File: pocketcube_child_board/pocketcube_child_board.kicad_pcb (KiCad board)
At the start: 2 copper layers, 50 x 50 mm, 7 parts, among them J1 M55-7102042R, U1 SI3477DV-T1-GE3

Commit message: Pushing Board sizes
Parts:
- removed the C1 at (99.2, 80.1)
- removed the J1 at (131.2, 82.3)
- removed the MOD1 at (110.7, 82.0)
- removed the U1 at (124.0, 68.5)
- added C1: 100nF, Capacitor_SMD:C_0402_1005Metric_Pad0.74x0.62mm_HandSolder, F.Cu at (125.3, 73.2)
- added C1: 100nF, Capacitor_SMD:C_0402_1005Metric_Pad0.74x0.62mm_HandSolder, F.Cu at (235.8, 63.3)
- added C2: 47uF, Capacitor_SMD:C_1206_3216Metric_Pad1.33x1.80mm_HandSolder, F.Cu at (225.1, 68.5)
- added C3: 47uF, Capacitor_SMD:C_1206_3216Metric_Pad1.33x1.80mm_HandSolder, F.Cu at (212.1, 59.7)
- added C4: 47uF, Capacitor_SMD:C_1206_3216Metric_Pad1.33x1.80mm_HandSolder, F.Cu at (220.3, 45.3)
- added C5: 47uF, Capacitor_SMD:C_1206_3216Metric_Pad1.33x1.80mm_HandSolder, F.Cu at (236.3, 52.0)
- added H1: MountingHole_Pad, MountingHole:MountingHole_2.2mm_M2_Pad_TopBottom, F.Cu at (204.3, 37.5)
- added H2: MountingHole_Pad, MountingHole:MountingHole_2.2mm_M2_Pad_TopBottom, F.Cu at (244.2, 37.5)
- added H3: MountingHole_Pad, MountingHole:MountingHole_2.2mm_M2_Pad_TopBottom, F.Cu at (204.3, 77.4)
- added H4: MountingHole_Pad, MountingHole:MountingHole_2.2mm_M2_Pad_TopBottom, F.Cu at (244.2, 77.4)
- added J1: M55-7102042R, inspirefly:HARWIN_M55-7102042R, F.Cu at (157.3, 75.4)
- added J1: M55-7102642R, inspirefly:HARWIN_M55-7102642R, F.Cu at (224.3, 74.8)
- added J2: M55-7101242R, inspirefly:HARWIN_M55-7101242R, F.Cu at (206.1, 55.5)
- added J3: M55-7101242R, inspirefly:HARWIN_M55-7101242R, F.Cu at (224.3, 39.3)
- added J4: M55-7101242R, inspirefly:HARWIN_M55-7101242R, F.Cu at (242.4, 55.5)
- added MOD1: RFM98W-433S2, inspirefly:XCVR_RFM98W-433S2, F.Cu at (224.1, 56.4)
- added MOD1: RFM98W-433S2, inspirefly:RFM98W-433S2, F.Cu at (136.8, 75.1)
- added R1: 100K, Resistor_SMD:R_0402_1005Metric_Pad0.72x0.64mm_HandSolder, F.Cu at (235.8, 61.3)
- added U1: SI3477DV-T1-GE3, inspirefly:SOT_V-T1-GE3_VIS, F.Cu at (150.1, 61.6)
- added U1: SI3477DV-T1-GE3, inspirefly:SOT_V-T1-GE3_VIS, F.Cu at (238.1, 67.6)
- AE1: moved to B.Cu
- moved AE1 107.4 mm to (202.1, 65.3), turned to -90 degrees
- moved R_BURN1 27.0 mm to (146.1, 61.8)
- moved R_PULLUP1 27.0 mm to (149.8, 64.1)
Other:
- board size 50 x 50 mm -> 133.6 x 52.6 mm
- board text added: "To +X"
- board text added: "To -X"
- board text added: "To -Y"
- board text added: "To Backplane"

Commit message: Antenna location changes
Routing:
- net GND: track 61.0 -> 55.9 mm, vias 40 -> 39
- added copper zone on In1.Cu, net GND
- added copper zone on In2.Cu, net GND
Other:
- copper layers 2 -> 4
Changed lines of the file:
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@@
 	(layers
 		(0 "F.Cu" signal)
+		(4 "In1.Cu" signal)
+		(6 "In2.Cu" signal)
 		(2 "B.Cu" signal)
 		(9 "F.Adhes" user "F.Adhesive")
@@
 	)
 	(setup
+		(stackup
+			(layer "F.SilkS"
+				(type "Top Silk Screen")
+			)
+			(layer "F.Paste"
+				(type "Top Solder Paste")
+			)
+			(layer "F.Mask"
+				(type "Top Solder Mask")
+				(thickness 0.01)
+			)
+			(layer "F.Cu"
+				(type "copper")
+				(thickness 0.035)
+			)
+			(layer "dielectric 1"
+				(type "prepreg")
+				(thickness 0.1)
+				(material "FR4")
+				(epsilon_r 4.5)
+				(loss_tangent 0.02)
+			)
+			(layer "In1.Cu"
+				(type "copper")
+				(thickness 0.035)
+			)
+			(layer "dielectric 2"
+				(type "core")
+				(thickness 1.24)
+				(material "FR4")
+				(epsilon_r 4.5)
+				(loss_tangent 0.02)
+			)
+			(layer "In2.Cu"
+				(type "copper")
+				(thickness 0.035)
+			)
+			(layer "dielectric 3"
+				(type "prepreg")
+				(thickness 0.1)
+				(material "FR4")
+				(epsilon_r 4.5)
+				(loss_tangent 0.02)
+			)
+			(layer "B.Cu"
+				(type "copper")
+				(thickness 0.035)
+			)
+			(layer "B.Mask"
+				(type "Bottom Solder Mask")
+				(thickness 0.01)
+			)
+			(layer "B.Paste"
+				(type "Bottom Solder Paste")
+			)
+			(layer "B.SilkS"
+				(type "Bottom Silk Screen")
+			)
+			(copper_finish "None")
+			(dielectric_constraints no)
+		)
 		(pad_to_mask_clearance 0)
 		(allow_soldermask_bridges_in_footprints no)
@@
 	)
 	(segment
-		(start 125.33 70.0825)
-		(end 124.53 70.0825)
-		(width 0.2)
-		(layer "F.Cu")
-		(net 3)
-	)
-	(segment
 		(start 122.63 65.0825)
 		(end 123.38 65.8325)
@@
 	)
 	(segment
-		(start 125.33 70.0825)
-		(end 125.33 72.5825)
-		(width 0.2)
-		(layer "F.Cu")
-		(net 3)
-	)
-	(segment
 		(start 151.5125 73.465)
 		(end 150.63 72.5825)
@@
 	)
 	(segment
-		(start 127.13 70.0825)
-		(end 125.33 70.0825)
-		(width 0.2)
-		(layer "F.Cu")
-		(net 3)
-	)
-	(segment
 		(start 146.88 65.8325)
 		(end 147.63 66.5825)
@@
 	)
 	(via
-		(at 124.53 70.0825)
-		(size 0.6)
-		(drill 0.3)
-		(layers "F.Cu" "B.Cu")
-		(free yes)
-		(net 3)
-	)
-	(via
 		(at 118.63 61.5825)
 		(size 0.6)
@@
 		(net 3)
 		(net_name "GND")
-		(layers "F.Cu" "B.Cu")
+		(layers "F.Cu" "B.Cu" "In1.Cu" "In2.Cu")
 		(hatch edge 0.5)
 		(priority 3)

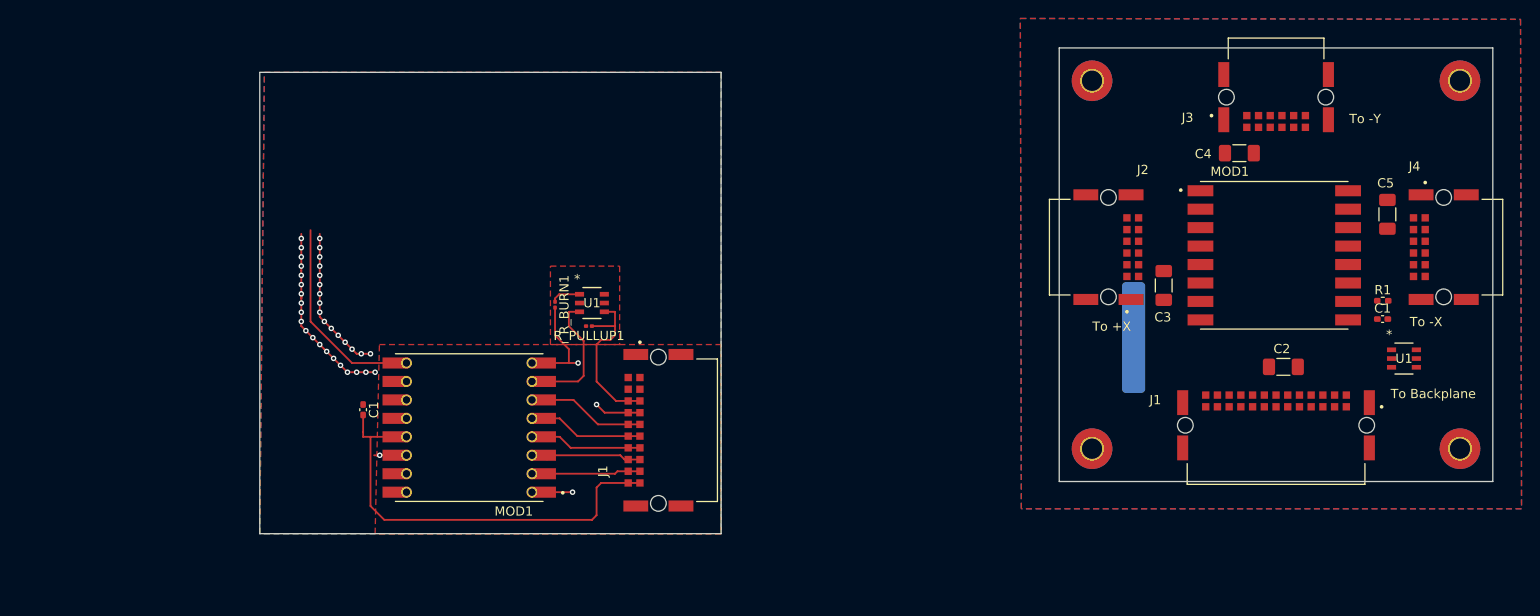
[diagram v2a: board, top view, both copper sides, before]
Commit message: updated antenna traces
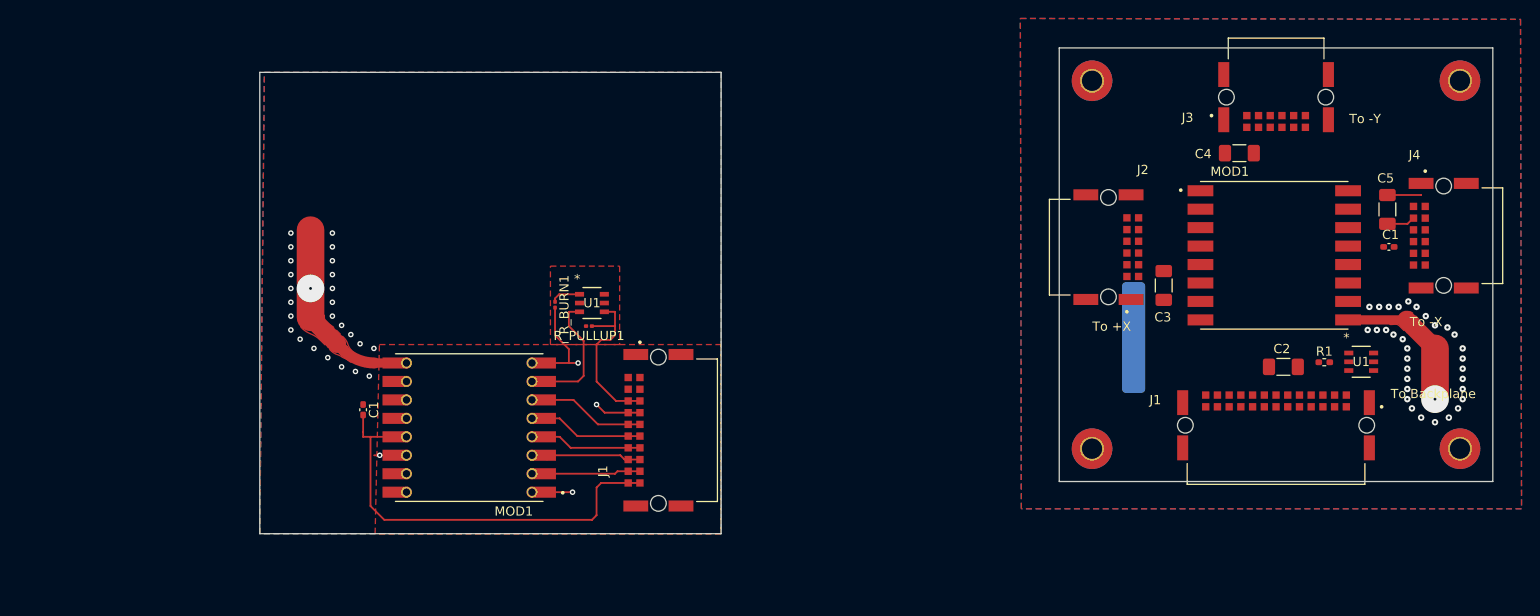
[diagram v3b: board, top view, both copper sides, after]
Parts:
- moved R1 9.20 mm to (229.5, 68.0)
- moved C1 7.85 mm to (236.5, 55.5)
- moved U1 4.65 mm to (233.5, 67.9)
- moved J4 1.24 mm to (242.4, 54.3)
- moved C5 0.53 mm to (236.3, 51.4)
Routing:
- net GND: track 55.9 -> 22.3 mm, vias 39 -> 60
- net /ANTENNA_TRACE: track 21.0 -> 37.8 mm, vias 0 -> 2
- net EXTERNAL_VOLTAGE: track 0.00 -> 3.10 mm
- added copper zone on F.Cu, net /ANTENNA_TRACE

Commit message: stuff from HITT
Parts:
- removed the C1 at (125.3, 73.2)
- removed the J1 at (157.3, 75.4)
- removed the MOD1 at (136.8, 75.1)
- removed R_BURN1: R, Resistor_SMD:R_0201_0603Metric
- removed R_PULLUP1: 10k, Resistor_SMD:R_0201_0603Metric
- removed the U1 at (150.1, 61.6)
- moved U1 3.65 mm to (237.2, 67.9)
- moved C1 2.00 mm to (236.5, 57.5)
- moved R1 1.80 mm to (230.5, 66.5)
- moved C5 1.50 mm to (236.3, 52.9)
- moved C2 1.13 mm to (223.9, 68.5)
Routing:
- net GND: track 22.3 -> 149.1 mm, vias 60 -> 13
- net 3.3V: track 46.6 -> 0.00 mm
- net /ANTENNA_TRACE: track 37.8 -> 0.00 mm, vias 2 -> 0
- net EXTERNAL_VOLTAGE: track 3.10 -> 24.0 mm
- net 4.2V: track 18.2 -> 0.00 mm
- net PMOS_GATE: track 13.4 -> 0.00 mm
- net MOSI: track 11.6 -> 0.00 mm
- net RFM_RESET: track 11.6 -> 0.00 mm
- net MISO: track 11.5 -> 0.00 mm
- net CS: track 11.3 -> 0.00 mm
- net CLK: track 11.0 -> 0.00 mm
- net BAT_VOLTAGE: track 0.00 -> 8.28 mm
- net Net-(R_BURN1-Pad1): track 3.20 -> 0.00 mm
- net +3.3V: track 0.00 -> 2.54 mm
- net unconnected-(MOD1-DIO0-Pad14): track 2.30 -> 0.00 mm, vias 1 -> 0
- removed copper zone on F.Cu, net /ANTENNA_TRACE
- removed copper zone on F.Cu, net 3.3V
- removed copper zone on F.Cu, net 4.2V
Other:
- board size 133.6 x 52.6 mm -> 47 x 47 mm

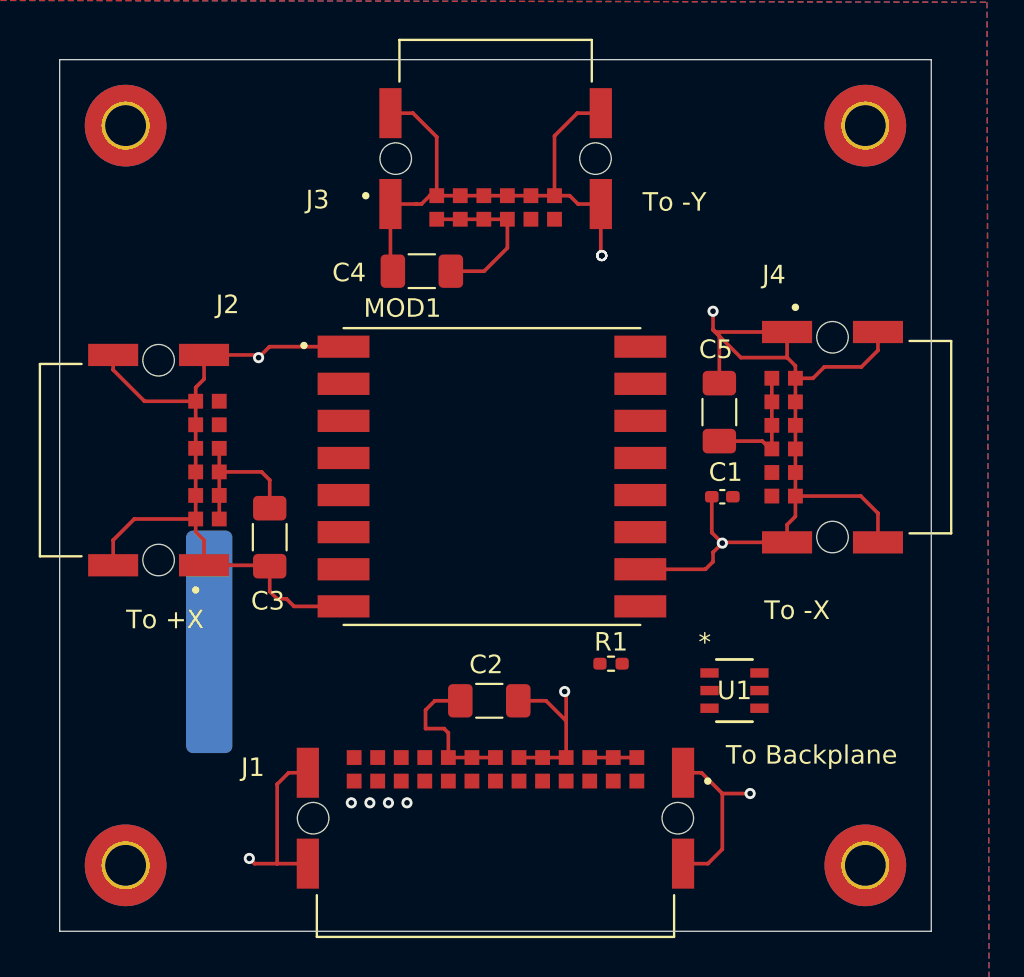
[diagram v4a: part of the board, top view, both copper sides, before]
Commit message: 4 layer board routing
2 ground layers between front and backplane to increase rf performance, may need to use for routing though
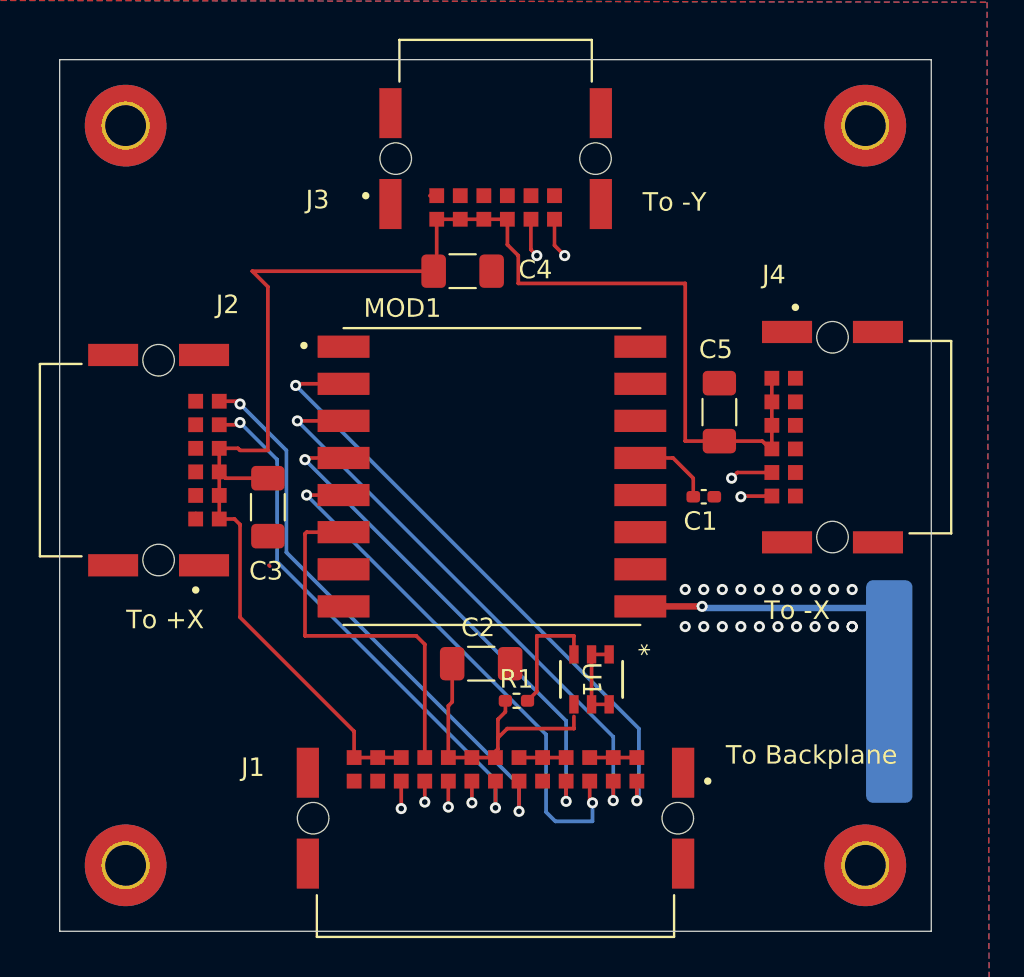
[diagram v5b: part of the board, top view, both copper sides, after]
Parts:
- moved AE1 50.2 mm to (252.2, 68.0), turned to 90 degrees
- moved U1 7.73 mm to (229.4, 67.3), turned to -90 degrees
- moved R1 5.48 mm to (225.4, 68.5)
- moved C4 2.20 mm to (222.5, 45.3), turned to 180 degrees
- moved C2 2.05 mm to (223.5, 66.5)
- moved C3 1.62 mm to (212.0, 58.1)
- moved C1 1.00 mm to (235.5, 57.5), turned to 180 degrees
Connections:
- J1 pad A1: ANT_SPI2_MOSI -> ANT_SPI2_MISO
- J1 pad A2: ANT_SPI2_MISO -> ANT_SPI2_MOSI
- J1 pad B10: EXTERNAL_VOLTAGE -> RFM_RESET
- J1 pad B13: RFM_RESET -> EXTERNAL_VOLTAGE
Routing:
- net GND: track 149.1 -> 3.94 mm, vias 13 -> 21
- net EXTERNAL_VOLTAGE: track 24.0 -> 84.5 mm
- net ANT_SPI2_MISO: track 0.00 -> 33.9 mm, vias 0 -> 2
- net ANT_SPI2_MOSI: track 0.00 -> 31.1 mm, vias 0 -> 2
- net I2C1_SDA: track 0.00 -> 31.0 mm, vias 0 -> 2
- net ANT_SPI2_NSS: track 0.00 -> 29.4 mm, vias 0 -> 2
- net I2C1_SCL: track 0.00 -> 29.1 mm, vias 0 -> 2
- net ANT_SPI2_SCK: track 0.00 -> 27.5 mm, vias 0 -> 2
- net RFM_RESET: track 0.00 -> 20.4 mm
- net /ANTENNA_TRACE: track 0.00 -> 15.6 mm, vias 0 -> 1
- net BAT_VOLTAGE: track 8.28 -> 15.9 mm
- net Net-(U1-G): track 0.00 -> 5.71 mm
- net Net-(R_BURN1-Pad1): track 0.00 -> 4.59 mm
- net 3.3V: track 0.00 -> 4.30 mm
- net I2C3_SCL: track 0.00 -> 3.78 mm, vias 0 -> 2
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
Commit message: Pushing Routing Changes
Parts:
- removed C2: 47uF, Capacitor_SMD:C_1206_3216Metric_Pad1.33x1.80mm_HandSolder
- removed R1: 100K, Resistor_SMD:R_0402_1005Metric_Pad0.72x0.64mm_HandSolder
- removed U1: SI3477DV-T1-GE3, inspirefly:SOT_V-T1-GE3_VIS
- moved C1 2.79 mm to (235.0, 54.8), turned to -90 degrees
- moved C4 2.70 mm to (219.8, 45.1), turned to 0 degrees
- moved C5 2.33 mm to (235.5, 50.8), turned to 90 degrees
- moved C3 1.33 mm to (212.0, 56.7), turned to -90 degrees
- moved AE1 0.28 mm to (252.5, 68.0)
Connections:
- C1 pad 2: 3.3V -> +3.3V
- J1 pad A1: ANT_SPI2_MISO -> ANT_SPI2_MOSI
- J1 pad A2: ANT_SPI2_MOSI -> ANT_SPI2_MISO
- J1 pad B10: RFM_RESET -> EXTERNAL_VOLTAGE
- J1 pad B13: EXTERNAL_VOLTAGE -> RFM_RESET
- MOD1 pad 13: 3.3V -> +3.3V
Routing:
- net EXTERNAL_VOLTAGE: track 84.5 -> 5.08 mm
- net I2C2_SDA: track 3.36 -> 45.3 mm
- net I2C2_SCL: track 3.49 -> 41.6 mm
- net I2C3_SCL: track 3.78 -> 36.6 mm
- net I2C3_SDA: track 2.82 -> 33.5 mm
- net ANT_SPI2_MOSI: track 31.1 -> 50.5 mm, vias 2 -> 4
- net ANT_SPI2_MISO: track 33.9 -> 52.6 mm
- net ANT_SPI2_SCK: track 27.5 -> 41.7 mm
- net BAT_VOLTAGE: track 15.9 -> 2.54 mm
- net I2C1_SDA: track 31.0 -> 43.2 mm
- net ANT_SPI2_NSS: track 29.4 -> 40.5 mm, vias 2 -> 4
- net I2C1_SCL: track 29.1 -> 39.6 mm
- net Net-(U1-G): track 5.71 -> 0.00 mm
- net RFM_RESET: track 20.4 -> 15.2 mm, vias 0 -> 2
- net Net-(R_BURN1-Pad1): track 4.59 -> 0.00 mm
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- added copper zone on F.Cu, net +3.3V
- added copper zone on F.Cu, net EXTERNAL_VOLTAGE

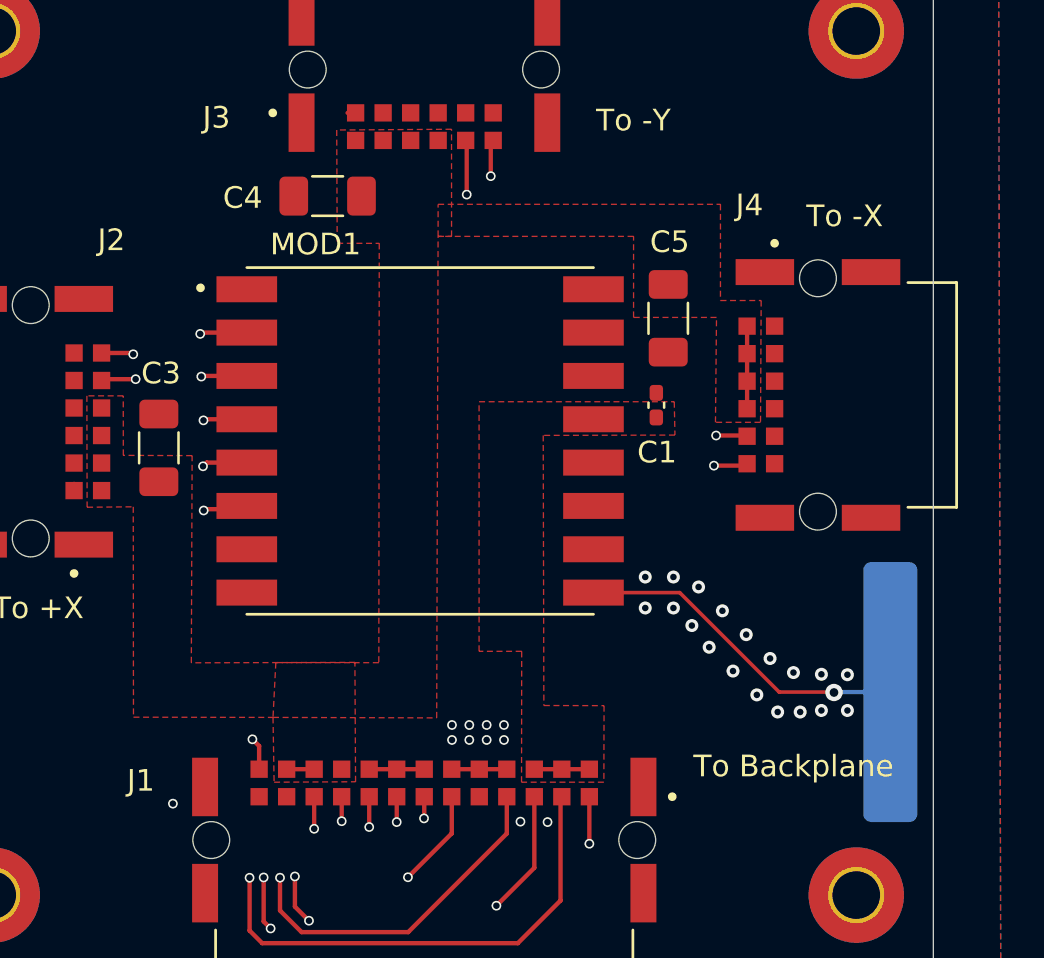
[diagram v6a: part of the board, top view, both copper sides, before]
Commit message: Updates due to changes from backplane
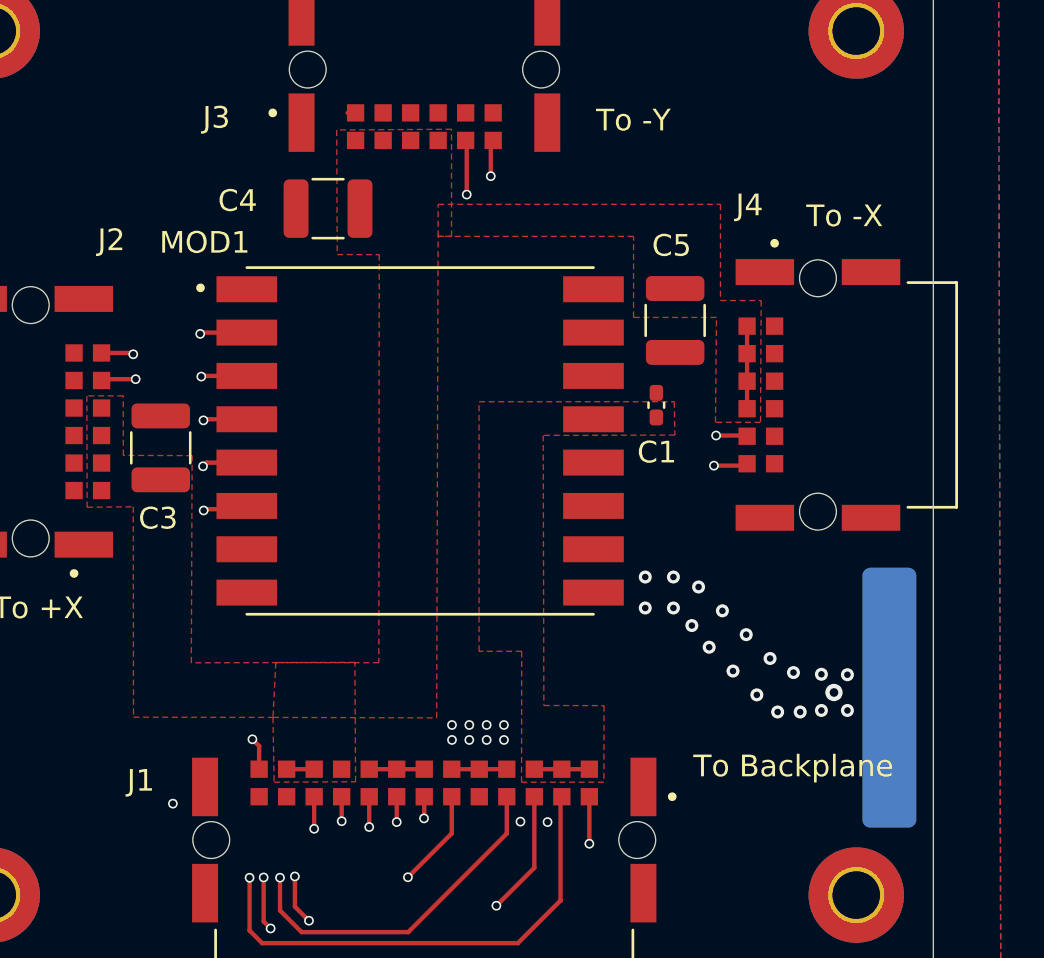
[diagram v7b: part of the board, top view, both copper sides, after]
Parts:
- C3, C4, C5: value 47uF -> 22uF; footprint Capacitor_SMD:C_1206_3216Metric_Pad1.33x1.80mm_HandSolder -> Capacitor_SMD:C_1210_3225Metric
- moved C4 0.58 mm to (219.8, 45.7)
- moved C5 0.34 mm to (235.8, 50.9)
- moved AE1 0.26 mm to (252.5, 68.3)
- moved C3 0.09 mm to (212.1, 56.7)

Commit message: BOM work + silkscreen
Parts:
- added G***: LOGO, LOGO, B.Cu at (223.4, 46.5)
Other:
- board text added: "Child Antenna PQ V0.1"
- board text added: "Larger Via to be left Untented"
